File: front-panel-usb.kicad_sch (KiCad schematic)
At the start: 87 parts, among them J2201 USB-C_Kycon_KUSBX-SL2-CS1N24-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, J2202 USB-C_Kycon_KUSBX-SL2-CS1N24-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, J2203 USB-C_Kycon_KUSBX-SL2-CS1N24-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, Q2201 PJE138K, U2201 AP22615B_TSOT26, U2202 FUSB303B, U2203 TPD4E05U06QDQARQ1, U2204 TPD4E05U06QDQARQ1, U2205 AP22615B_TSOT26, U2206 HD3SS3220RNH, U2207 TPD4E05U06QDQARQ1, U2208 74LVC06ABQ, U2209 TPD4E05U06QDQARQ1, U2210 TPD4E05U06QDQARQ1, U2211 74AUP2G132

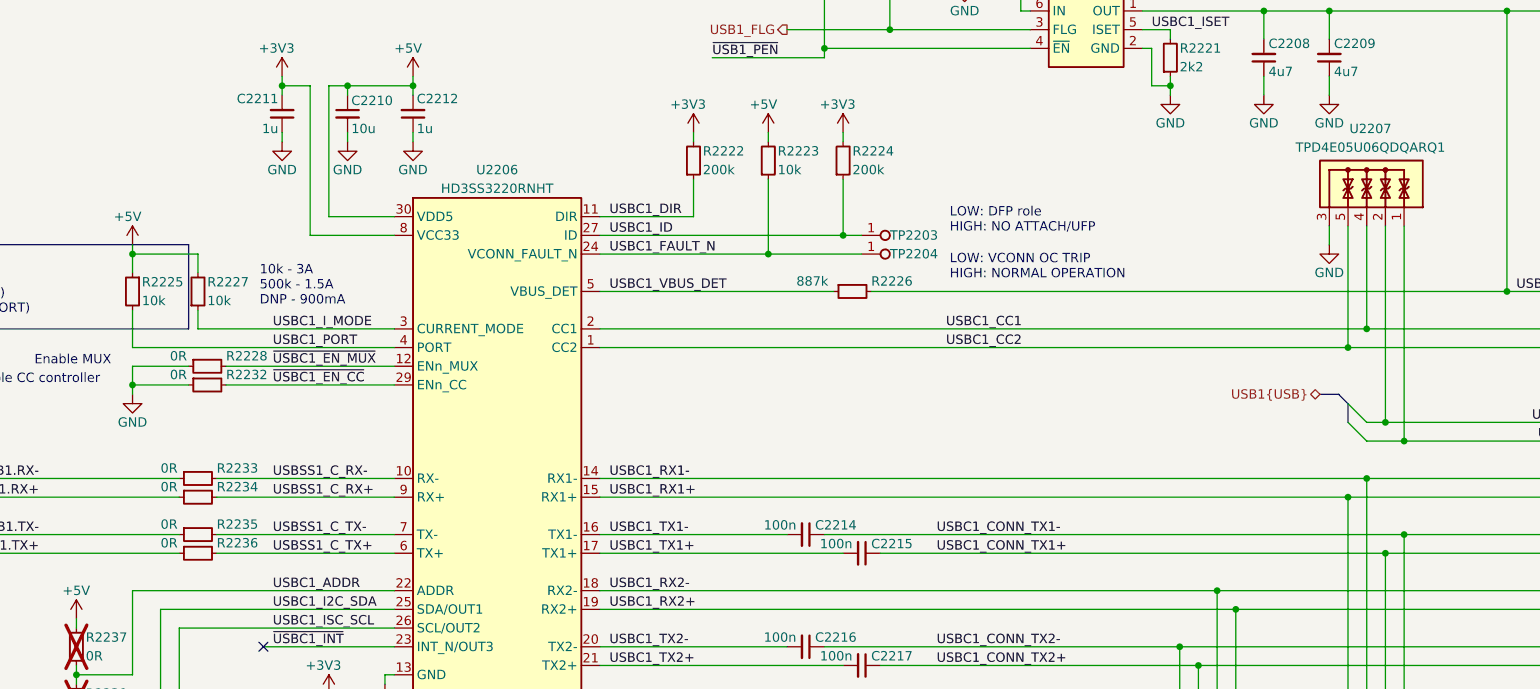
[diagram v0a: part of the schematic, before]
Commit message: [#100063] Modify DP and USB connections to optimize routing
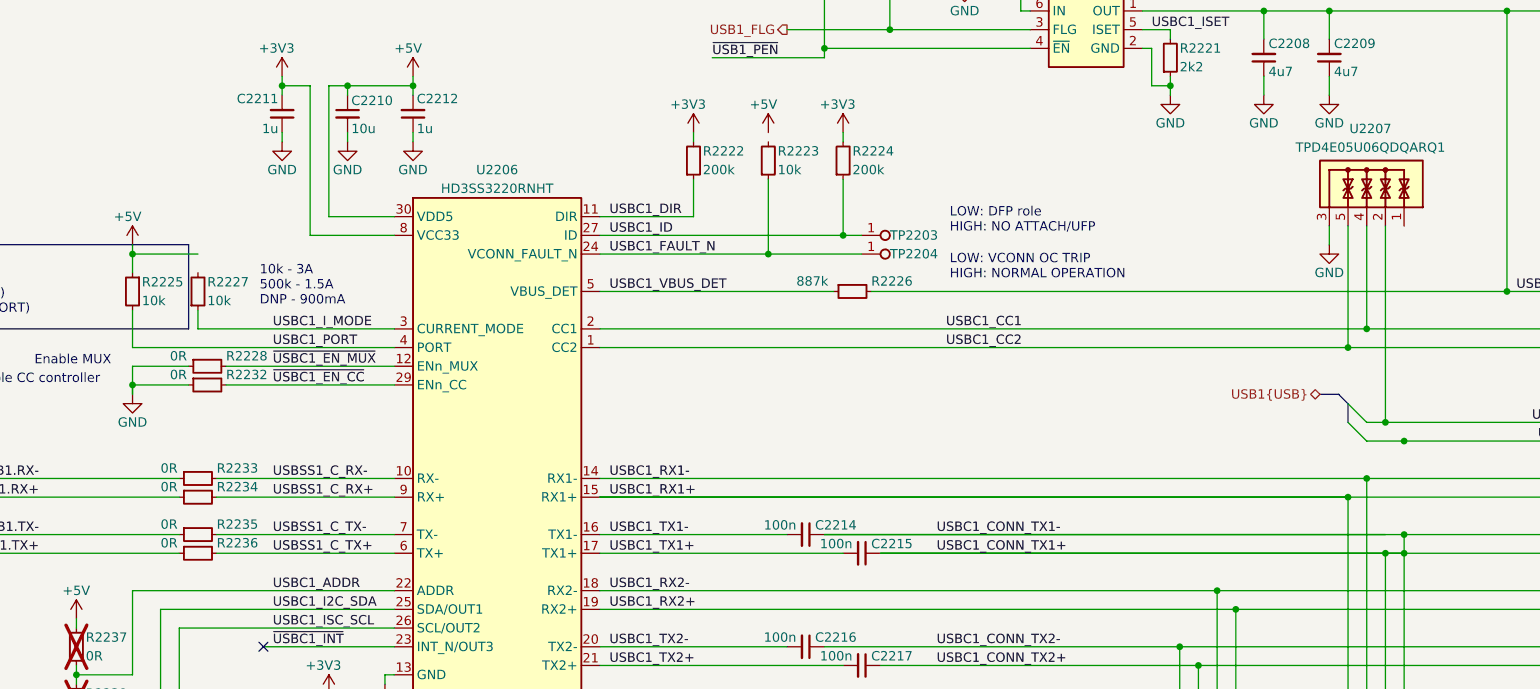
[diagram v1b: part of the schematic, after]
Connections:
- net USBC1_CONN_TX1- is gone; now on net USBC1_CONN_TX1+: C2214.1, J2203.A2 (TX_{1}+), U2210.1, U2210.10
- net +5V: no longer R2223.2, R2227.2
- net USB1.D-: no longer U2207.1, U2207.10
- new net: U2207.1, U2207.10
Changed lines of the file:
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@@
+	)
+	(junction
+		(at 349.25 207.01)
+		(diameter 0)
+		(color 0 0 0 0)
 	)
 	(junction
@@
 	(wire
 		(pts
+			(xy 278.13 207.01) (xy 349.25 207.01)
+		)
+		(stroke
+			(width 0)
+			(type default)
+		)
+	)
+	(wire
+		(pts
 			(xy 182.88 217.17) (xy 182.88 228.6)
 		)
@@
 	(wire
 		(pts
-			(xy 185.42 166.37) (xy 185.42 168.91)
-		)
-		(stroke
-			(width 0)
-			(type default)
-		)
-	)
-	(wire
-		(pts
 			(xy 270.51 120.65) (xy 270.51 123.19)
 		)
@@
 	(wire
 		(pts
+			(xy 270.51 204.47) (xy 346.71 204.47)
+		)
+		(stroke
+			(width 0)
+			(type default)
+		)
+	)
+	(wire
+		(pts
 			(xy 240.03 219.71) (xy 265.43 219.71)
 		)
@@
 	(wire
 		(pts
-			(xy 349.25 162.56) (xy 349.25 191.77)
+			(xy 176.53 184.15) (xy 176.53 185.42)
 		)
 		(stroke
@@
 	(wire
 		(pts
+			(xy 240.03 199.39) (xy 341.63 199.39)
+		)
+		(stroke
+			(width 0)
+			(type default)
+		)
+	)
+	(wire
+		(pts
 			(xy 311.15 26.67) (xy 320.04 26.67)
 		)
 		(stroke
-			(width 0)
-			(type default)
-		)
-	)
-	(wire
-		(pts
-			(xy 262.89 149.86) (xy 262.89 151.13)
-		)
-		(stroke

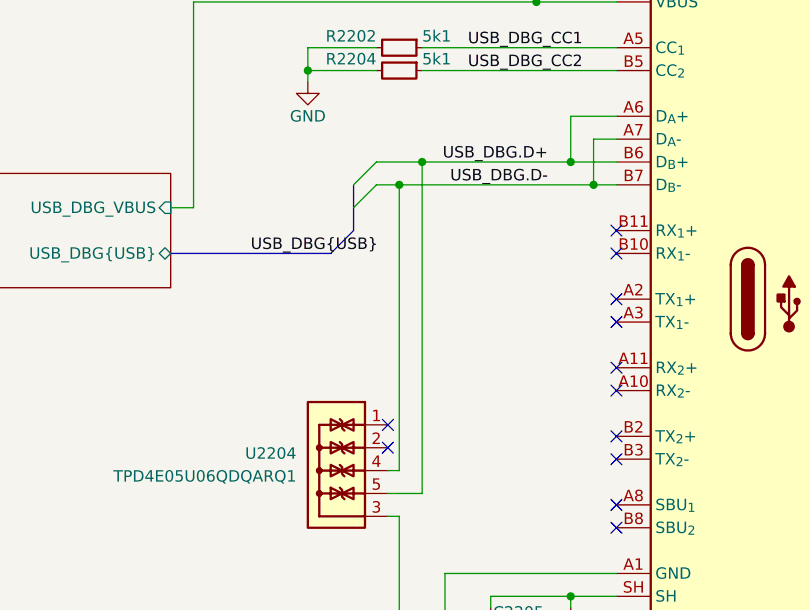
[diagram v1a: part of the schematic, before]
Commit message: [#100063] Modify DP and USB connections to optimize routing
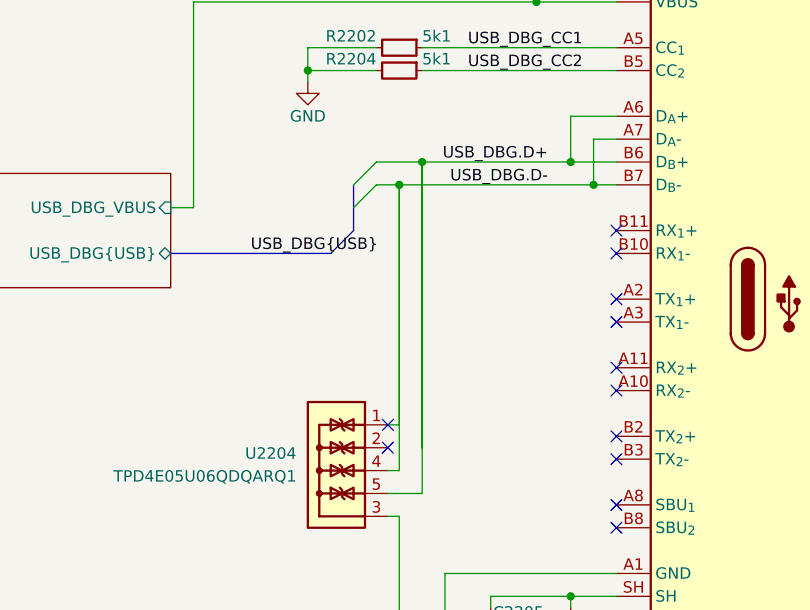
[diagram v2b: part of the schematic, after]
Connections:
- net USB_DBG.D-: now also U2204.1, U2204.10
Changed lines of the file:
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@@
+	(wire
+		(pts
+			(xy 119.38 44.45) (xy 119.38 76.2)
+		)
+		(stroke
+			(width 0)
+			(type default)
+		)
+	)
 	(wire
 		(pts
@@
 	(wire
 		(pts
+			(xy 116.84 46.99) (xy 116.84 73.66)
+		)
+		(stroke
+			(width 0)
+			(type default)
+		)
+	)
+	(wire
+		(pts
 			(xy 203.2 231.14) (xy 203.2 228.6)
 		)
@@
 		)
 		(stroke
+			(width 0)
+			(type default)
+		)
+	)
+	(wire
+		(pts
+			(xy 116.84 73.66) (xy 115.57 73.66)
+		)
+		(stroke

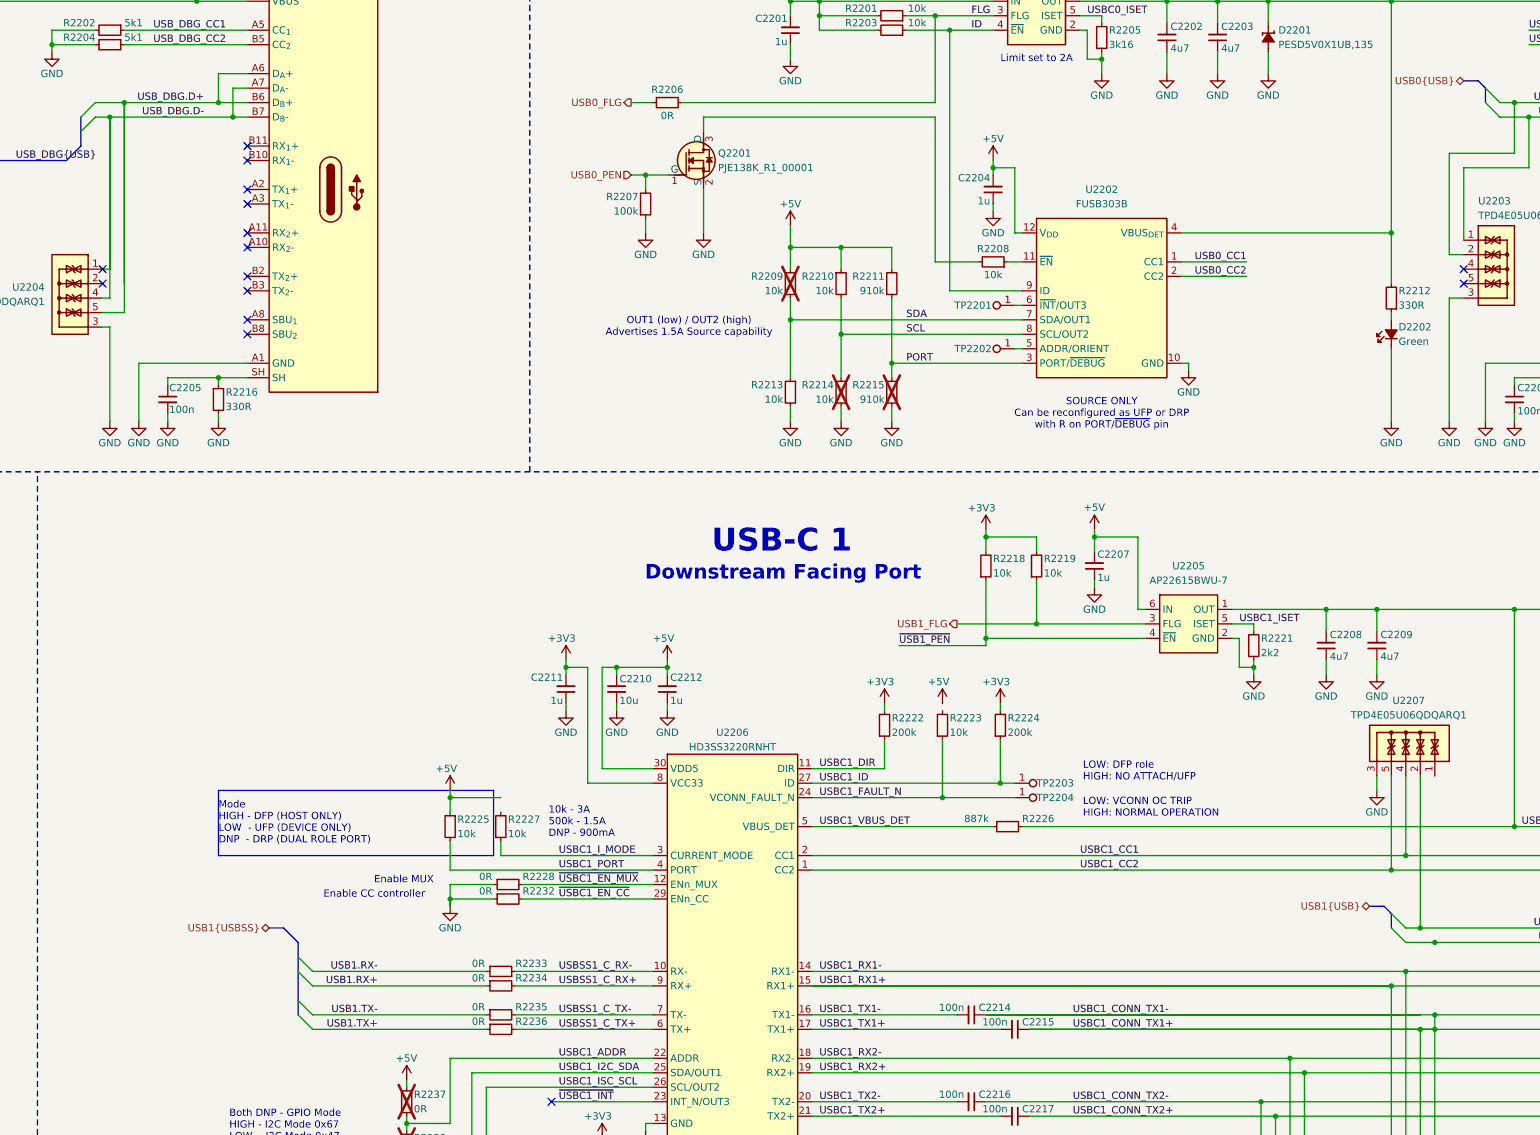
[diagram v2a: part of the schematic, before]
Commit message: [#100063] Continue routing, mainly USB-C and DP connector
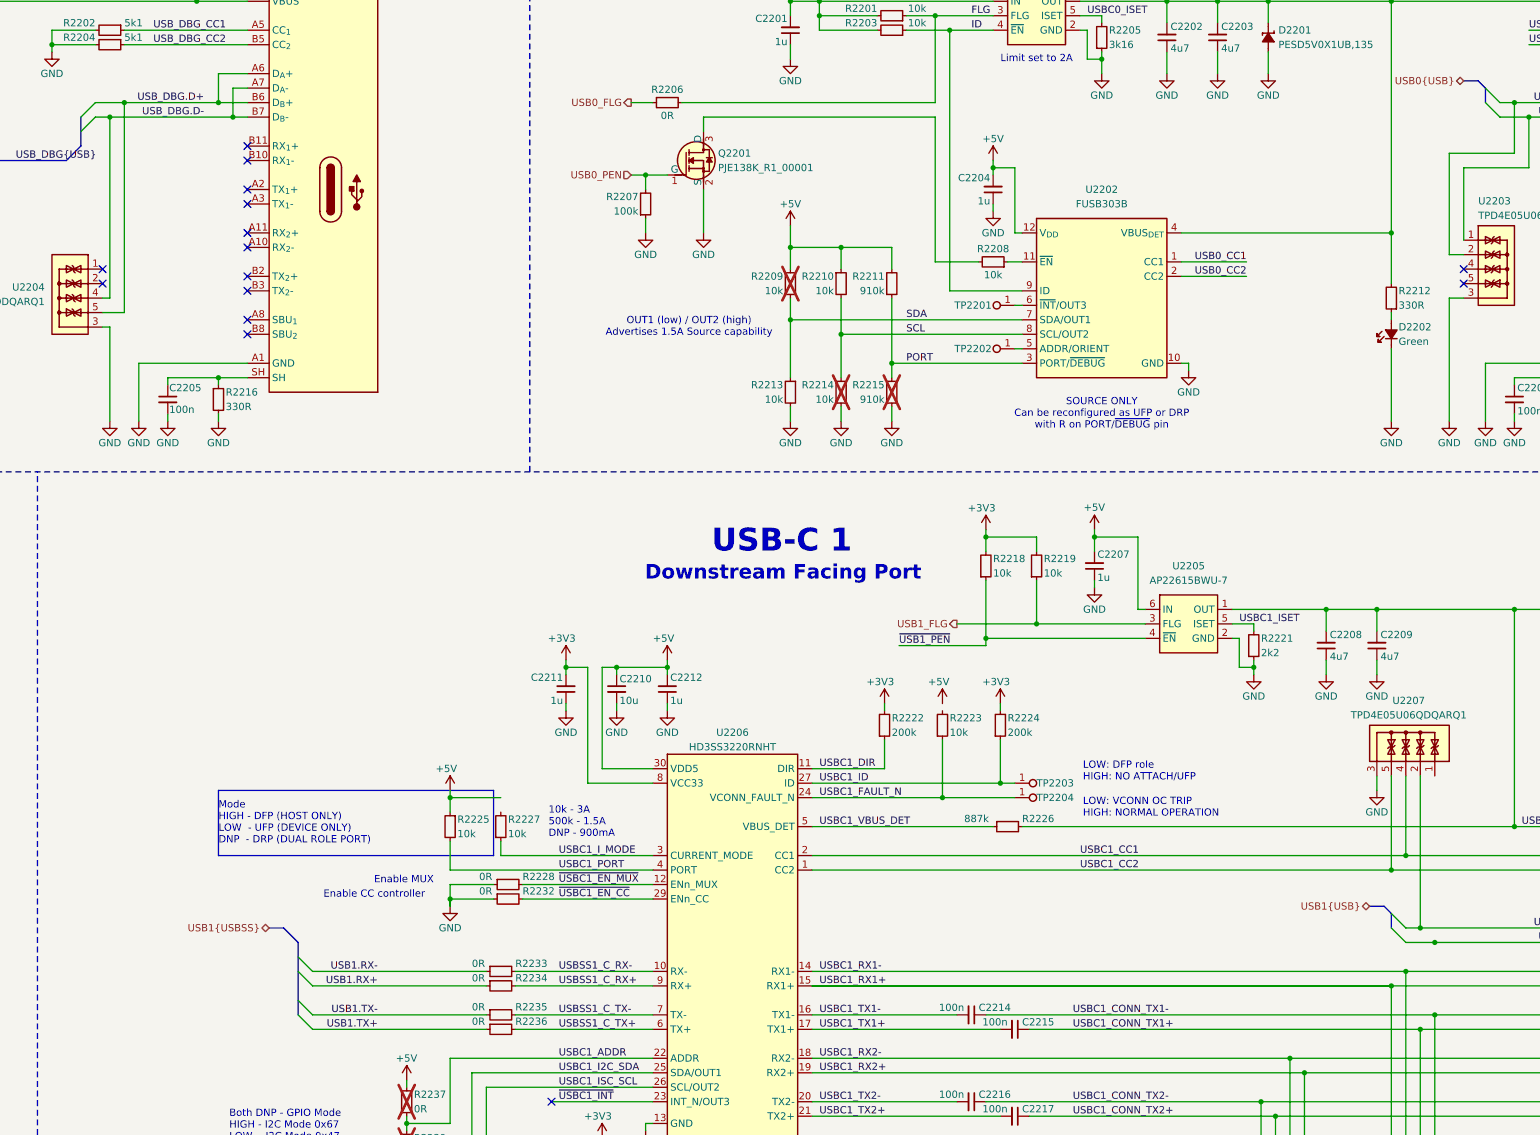
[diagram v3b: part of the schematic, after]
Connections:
- net USBC1_CONN_TX1+: no longer C2214.1, J2203.A2 (TX_{1}+), U2210.1, U2210.10
- net USB_DBG.D-: no longer U2204.1, U2204.10
- new net: U2204.1, U2204.10
- new net USBC1_CONN_TX1-: C2214.1, J2203.A2 (TX_{1}+), U2210.1, U2210.10
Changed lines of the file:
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@@
-	)
-	(junction
-		(at 349.25 207.01)
-		(diameter 0)
-		(color 0 0 0 0)
 	)
 	(junction
@@
 	(wire
 		(pts
-			(xy 278.13 207.01) (xy 349.25 207.01)
-		)
-		(stroke
-			(width 0)
-			(type default)
-		)
-	)
-	(wire
-		(pts
 			(xy 182.88 217.17) (xy 182.88 228.6)
 		)
@@
 	(wire
 		(pts
-			(xy 119.38 44.45) (xy 119.38 76.2)
-		)
-		(stroke
-			(width 0)
-			(type default)
-		)
-	)
-	(wire
-		(pts
 			(xy 185.42 173.99) (xy 185.42 176.53)
 		)
@@
 	(wire
 		(pts
-			(xy 270.51 204.47) (xy 346.71 204.47)
-		)
-		(stroke
-			(width 0)
-			(type default)
-		)
-	)
-	(wire
-		(pts
 			(xy 240.03 219.71) (xy 265.43 219.71)
 		)
@@
 	(wire
 		(pts
-			(xy 116.84 46.99) (xy 116.84 73.66)
-		)
-		(stroke
-			(width 0)
-			(type default)
-		)
-	)
-	(wire
-		(pts
 			(xy 203.2 231.14) (xy 203.2 228.6)
 		)
@@
 		)
 		(stroke
-			(width 0)
-			(type default)
-		)
-	)
-	(wire
-		(pts
-			(xy 116.84 73.66) (xy 115.57 73.66)
-		)
-		(stroke

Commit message: [#100501] Change USB-C 1 port current from 3A to 1.5A
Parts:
- removed R2205: R_3k16_0402, antmicro-footprints:R_0402_1005Metric, symbol antmicroResistors0402:R_3k16_0402
- removed R2221: R_2k2_0402, antmicro-footprints:R_0402_1005Metric, symbol antmicroResistors0402:R_2k2_0402
- removed R2227: R_10k_0402, antmicro-footprints:R_0402_1005Metric, symbol antmicroResistors0402:R_10k_0402
- added R2205: R_499k_0402, antmicro-footprints:R_0402_1005Metric, symbol antmicroResistors0402:R_499k_0402
- added R2221, R2227: R_4k3_0402, antmicro-footprints:R_0402_1005Metric, symbol antmicroResistors0402:R_4k3_0402
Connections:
- net +5V: now also R2223.2, R2205.2
- net GND: now also R2221.1, R2227.1
- net USB1.D-: now also U2207.1, U2207.10
- net USBC0_ISET: now also R2221.2
- net USBC1_ISET: now also R2227.2
- net USBC1_I_MODE: now also R2205.1

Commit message: [#100501] Reannotate schematic
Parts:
- renumbered C2201 to C206, C2202 to C207, C2203 to C208, C2204 to C209, C2205 to C210, C2206 to C211, C2207 to C212, C2208 to C213, C2209 to C214, C2210 to C215, C2211 to C216, C2212 to C217, C2213 to C218, C2214 to C219, C2215 to C220, C2216 to C221, C2217 to C222, C2218 to C223, C2219 to C224, D2205 to D10, D2206 to D11, D2207 to D12, D2201 to D6, D2202 to D7, D2203 to D8, D2204 to D9, H2201 to H5, J2203 to J10, J2201 to J8, J2202 to J9, Q2201 to Q7, R2201 to R254, R2202 to R255, R2203 to R256, R2204 to R257, R2221 to R258, R2206 to R259, R2207 to R260, R2208 to R261, R2209 to R262, R2210 to R263, R2211 to R264, R2212 to R265, R2213 to R266, R2214 to R267, R2215 to R268, R2216 to R269, R2217 to R270, R2218 to R271, R2219 to R272, R2220 to R273, R2227 to R274, R2222 to R275, R2223 to R276, R2224 to R277, R2225 to R278, R2226 to R279, R2205 to R280, R2228 to R281, R2229 to R282, R2230 to R283, R2231 to R284, R2232 to R285, R2233 to R286, R2234 to R287, R2235 to R288, R2236 to R289, R2237 to R290, R2238 to R291, R2239 to R292, R2240 to R293, R2241 to R294, TP2201 to TP25, TP2202 to TP26, TP2203 to TP27, TP2204 to TP28, U2201 to U29, U2202 to U30, U2203 to U31, U2204 to U32, U2205 to U33, U2206 to U34, U2207 to U35, U2208 to U36, U2209 to U37, U2210 to U38, U2211 to U39

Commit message: [#100501] Add Tag-Connect to JTAG and config EEPROM to FTDI, connect DC-SCM USB1 to USB controller
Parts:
- added TP30, TP31: TP_0.75mm_SMD, antmicro-footprints:TP_SMD_0.75mm, symbol antmicroTestPoints:TP_0.75mm_SMD
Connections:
- net USBC1_I2C_SDA: now also TP31.1
- net USBC1_ISC_SCL: now also TP30.1
- net SCL renamed OUT2
- net SDA renamed OUT1
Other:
- sheet FTDI ports: added ~{RESET}; removed none
- note added: "I_{LIM} = 6800/R I_{LIM} = 1.58 A"
- note added: "SOURCE ONLY"
- note removed: "Limit set to 2A"
- note removed: "SOURCE ONLY Can be reconfigured as UFP or DRP with R on PORT/~{DEBUG} pin"

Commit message: [#100501] Reannotate schematic
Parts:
- renumbered C206 to C197, C207 to C198, C208 to C199, C209 to C200, C210 to C201, C211 to C202, C212 to C203, C213 to C204, C214 to C205, C215 to C206, C216 to C207, C217 to C208, C218 to C209, C219 to C210, C220 to C211, C221 to C212, C222 to C213, C223 to C214, C224 to C215, D6 to D11, D7 to D12, D8 to D13, D9 to D14, D10 to D15, D11 to D16, D12 to D17, J9 to J10, J10 to J11, J8 to J9, Q7 to Q9, R254 to R279, R255 to R280, R256 to R281, R257 to R282, R258 to R283, R259 to R284, R260 to R285, R261 to R286, R262 to R287, R263 to R288, R264 to R289, R265 to R290, R266 to R291, R267 to R292, R268 to R293, R269 to R294, R270 to R295, R271 to R296, R272 to R297, R273 to R298, R274 to R299, R275 to R300, R276 to R301, R277 to R302, R278 to R303, R279 to R304, R280 to R305, R281 to R306, R282 to R307, R283 to R308, R284 to R309, R285 to R310, R286 to R311, R287 to R312, R288 to R313, R289 to R314, R290 to R315, R291 to R316, R292 to R317, R293 to R318, R294 to R319, TP25 to TP29, TP26 to TP30, TP27 to TP31, TP28 to TP32, TP30 to TP33, TP31 to TP34, U29 to U26, U30 to U27, U31 to U28, U32 to U29, U33 to U30, U34 to U31, U35 to U32, U36 to U33, U37 to U34, U38 to U35, U39 to U36
